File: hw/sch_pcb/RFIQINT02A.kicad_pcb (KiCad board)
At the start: 2 copper layers, 40.1 x 60.5 mm, 33 parts, among them J1 HEADER_2x03_PARALLEL, J2 HEADER_2x04_PARALLEL, J3 SATA7-67491-1030, J4 SATA7-67491-1030, J5 SATA7-67491-1030, J6 RJ45_RJHSE-5384, J7 RJ45_RJHSE-5384, M1 HOLE, M2 HOLE, M3 HOLE, M4 HOLE, U1 Si53322

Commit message: Edit PCB
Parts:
- J1, J2, J3, J4, J5, J6, J7: moved to B.Cu
- moved M2 166.2 mm to (5.08, -55.9)
- moved C10 151.8 mm to (30.5, -53.0), turned to 90 degrees
- moved C1 150.8 mm to (10.3, -47.1), turned to 90 degrees
- moved C9 150.5 mm to (14.9, -40.7), turned to 90 degrees
- moved U1 149.0 mm to (13.1, -32.3)
- moved L1 148.3 mm to (9.84, -25.4)
- moved J2 148.3 mm to (4.95, -45.7)
- moved C8 147.9 mm to (17.4, -40.7), turned to 90 degrees
- moved R4 146.7 mm to (18.4, -37.2)
- moved D2 145.7 mm to (10.2, -38.6), turned to -90 degrees
- moved C5 144.7 mm to (9.97, -27.6), turned to 180 degrees
- moved D1 143.8 mm to (5.08, -34.3), turned to 90 degrees
- moved C7 142.2 mm to (21.5, -32.1)
- moved R2 141.6 mm to (18.7, -28.6), turned to -90 degrees
- moved R6 140.7 mm to (35.2, -50.8)
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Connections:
- C6 pad 2: /CLKOUT0_P -> /CLKOUT1_P
- C7 pad 2: /CLKOUT0_N -> /CLKOUT1_N
- C8 pad 2: /CLKOUT1_P -> /CLKOUT0_P
- C9 pad 2: /CLKOUT1_N -> /CLKOUT0_N
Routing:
- net VCC: track 0.00 -> 57.1 mm, vias 0 -> 3
- net /ADC4_P: track 0.00 -> 31.0 mm
- net /ADC1_P: track 0.00 -> 27.7 mm, vias 0 -> 1
- net /ADC4_N: track 0.00 -> 27.6 mm
- net /ADC3_P: track 0.00 -> 26.6 mm, vias 0 -> 1
- net /ADC1_N: track 0.00 -> 25.4 mm, vias 0 -> 1
- net /ADC3_N: track 0.00 -> 25.0 mm, vias 0 -> 1
- net /CLKOUT1_P: track 0.00 -> 20.5 mm
- net /ADC2_P: track 0.00 -> 19.4 mm, vias 0 -> 1
- net /ADC2_N: track 0.00 -> 18.1 mm, vias 0 -> 1
- net /CLKOUT0_P: track 0.00 -> 16.4 mm
- net /CLKOUT1_N: track 0.00 -> 16.3 mm
- net /CLKOUT0_N: track 0.00 -> 16.2 mm
- net Net-(D1-Pad1): track 0.00 -> 14.1 mm
- net Net-(C8-Pad1): track 0.00 -> 8.95 mm
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
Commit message: Edit PCB
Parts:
- C1, C10, C11, C2, C3, C4, C5, C6, C7, C8, C9, D1, D2, L1, M2, M4, R1, R2, R3, R4, R5, R6, R7, U1: moved to B.Cu
- J1, J2, J3, J4, J5, J6, J7: moved to F.Cu
- moved M4 164.7 mm to (5.08, -55.8)
- moved J5 54.5 mm to (16.5, -57.7)
- moved M2 50.9 mm to (5.08, -4.97)
- moved J4 47.1 mm to (16.5, -6.88)
- moved C10 45.2 mm to (30.5, -7.83), turned to -90 degrees
- moved R6 40.7 mm to (35.2, -10.1)
- moved J6 34.4 mm to (34.9, -13.2), turned to 90 degrees
- moved C1 33.4 mm to (10.3, -13.7), turned to -90 degrees
- moved J2 30.6 mm to (4.95, -15.1)
- moved J3 24.8 mm to (16.0, -42.8)
- moved C8 20.6 mm to (17.4, -20.1), turned to -90 degrees
- moved C9 20.6 mm to (14.9, -20.1), turned to -90 degrees
- moved D2 16.4 mm to (10.2, -22.2), turned to 90 degrees
- moved C2 15.8 mm to (10.8, -38.3), turned to 90 degrees
- moved C3 14.4 mm to (13.6, -37.6), turned to -90 degrees
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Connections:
- M4 pad 1: Net-(M4-Pad1) -> GND
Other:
- board text added: "ADC 1,2"
- board text added: "ADC 3,4"
- board text added: "CLK"
- board text added: "POWER IN 3V3"
- board text added: "POWER IN ANT"

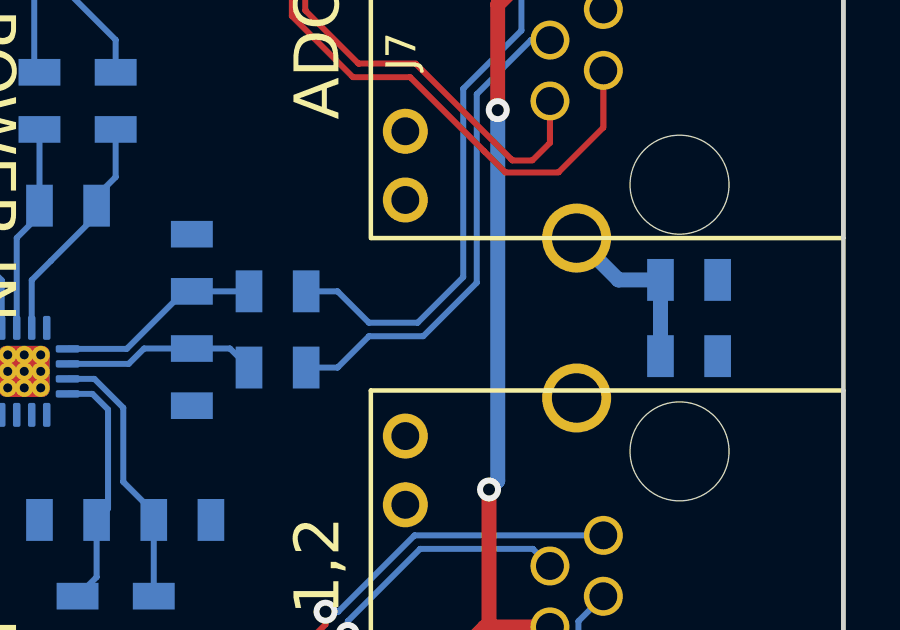
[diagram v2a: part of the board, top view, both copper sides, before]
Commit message: Test of differential pair skew tune.
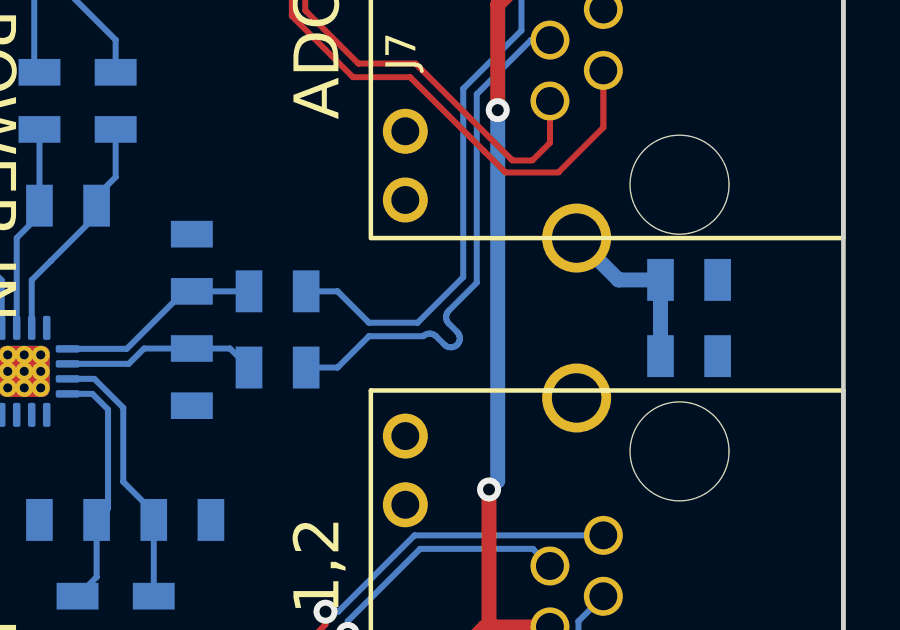
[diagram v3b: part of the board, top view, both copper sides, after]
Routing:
- net /CLKOUT1_N: track 16.3 -> 17.8 mm

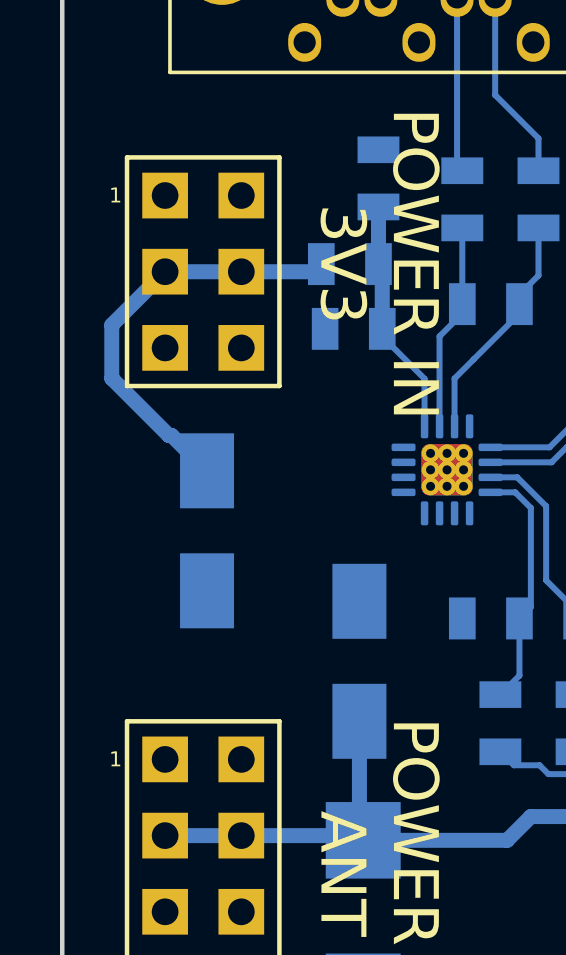
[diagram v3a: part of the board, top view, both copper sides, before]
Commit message: Improve documentation. Generate new image. Remove irrelavant symbols in silkscreen.
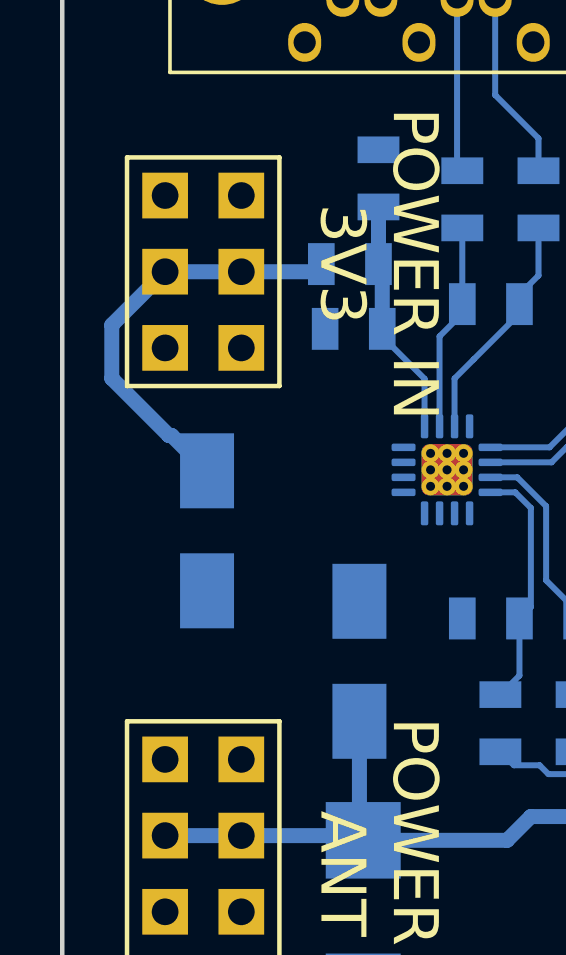
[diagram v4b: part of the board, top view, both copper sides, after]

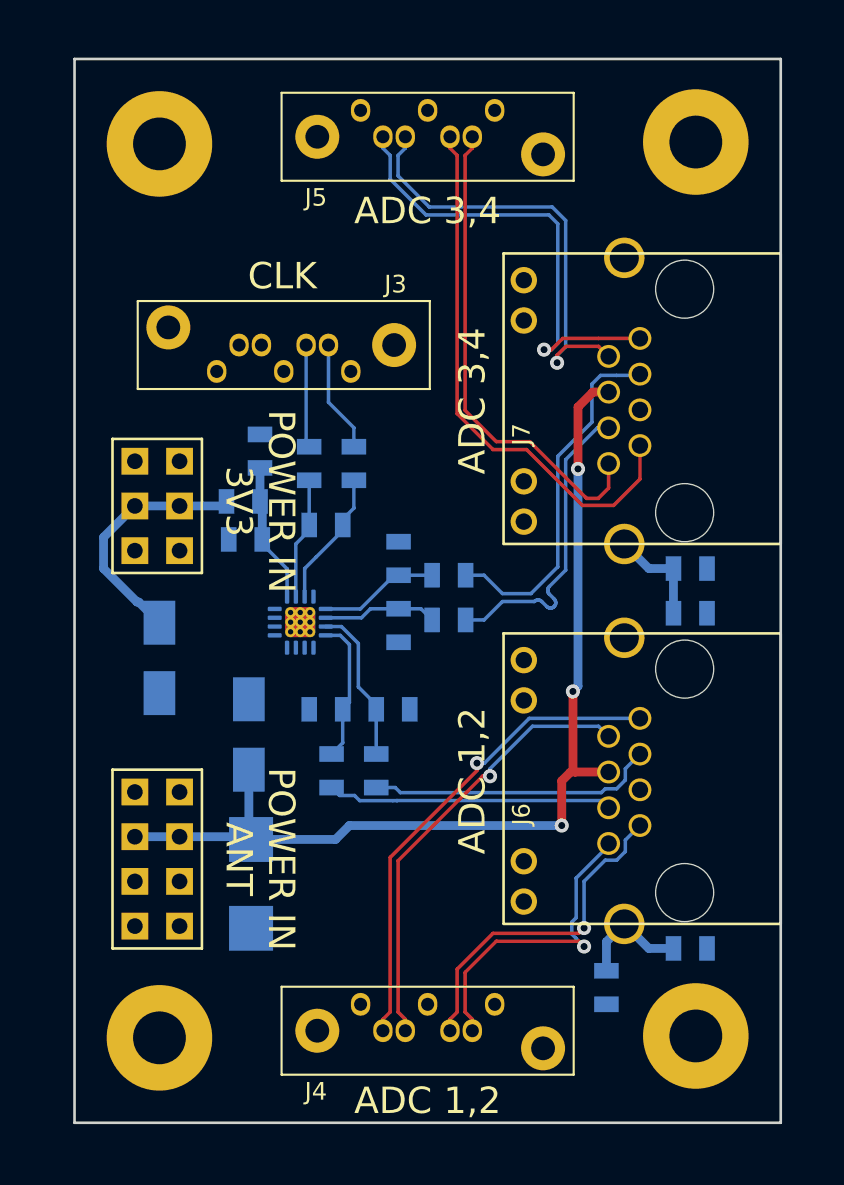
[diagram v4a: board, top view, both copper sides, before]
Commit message: remove vias from differential pairs routing.
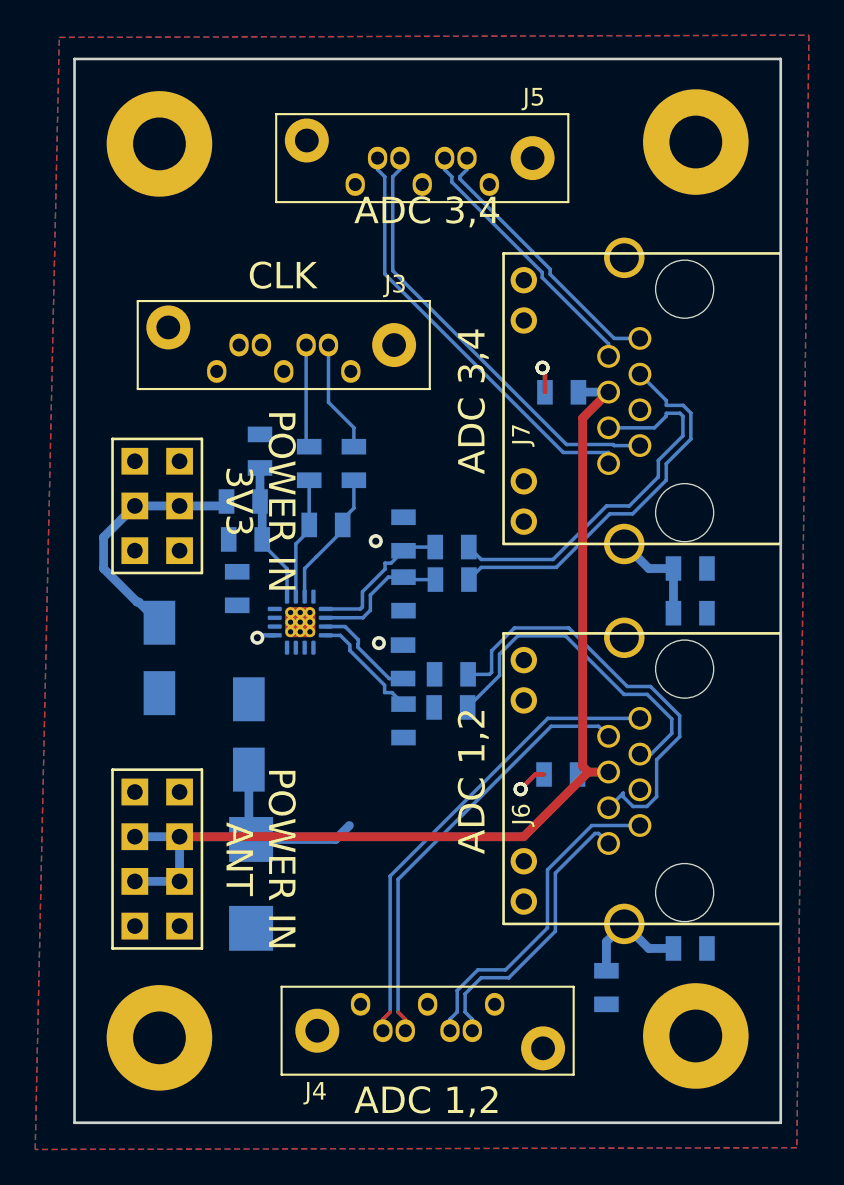
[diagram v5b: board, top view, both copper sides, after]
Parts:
- added C12: 100nF, Mlab_R:SMD-0805, B.Cu at (27.9, -19.9)
- added C13: 100nF, Mlab_R:SMD-0805, B.Cu at (27.9, -41.7)
- added C14: 1uF, Mlab_R:SMD-0805, B.Cu at (9.50, -30.5)
- moved J5 8.44 mm to (23.8, -53.5), turned to 0 degrees
- moved C9 7.68 mm to (21.6, -23.7), turned to 0 degrees
- moved C8 6.94 mm to (21.7, -25.6), turned to 0 degrees
- moved R5 4.46 mm to (18.9, -23.0), turned to -90 degrees
- moved R4 2.76 mm to (18.9, -26.3), turned to 90 degrees
- moved C7 2.30 mm to (21.7, -31.0)
- moved R3 1.82 mm to (18.9, -30.2)
- moved C6 1.61 mm to (21.7, -32.9)
- moved R2 1.42 mm to (18.9, -33.6)
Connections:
- net Net-(C3-Pad1) renamed /CLKIN_P
- net Net-(C3-Pad2) renamed /CLK_P
- net Net-(C4-Pad1) renamed /CLKIN_N
- net Net-(C4-Pad2) renamed /CLK_N
- net Net-(C6-Pad1) renamed /Q0_P
- net Net-(C7-Pad1) renamed /Q0_N
- net Net-(C8-Pad1) renamed /Q1_P
- net Net-(C9-Pad1) renamed /Q1_N
- J3 pad 5: Net-(J3-Pad5) -> unconnected-(J3-Pad5)
- J3 pad 6: Net-(J3-Pad6) -> unconnected-(J3-Pad6)
- J6 pad 10: Net-(J6-Pad10) -> unconnected-(J6-Pad10)
- J6 pad 11: Net-(J6-Pad11) -> unconnected-(J6-Pad11)
- J6 pad 12: Net-(J6-Pad12) -> unconnected-(J6-Pad12)
- J6 pad 3: /CLKOUT0_P -> /CLKOUT0_N
- J6 pad 6: /CLKOUT0_N -> /CLKOUT0_P
- J6 pad 9: Net-(J6-Pad9) -> unconnected-(J6-Pad9)
- J7 pad 10: Net-(J7-Pad10) -> unconnected-(J7-Pad10)
- J7 pad 11: Net-(J7-Pad11) -> unconnected-(J7-Pad11)
- J7 pad 12: Net-(J7-Pad12) -> unconnected-(J7-Pad12)
- J7 pad 3: /CLKOUT1_P -> /CLKOUT1_N
- J7 pad 6: /CLKOUT1_N -> /CLKOUT1_P
- J7 pad 9: Net-(J7-Pad9) -> unconnected-(J7-Pad9)
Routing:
- net VCC: track 57.1 -> 73.5 mm, vias 3 -> 0
- net /ADC3_P: track 26.6 -> 15.5 mm, vias 1 -> 0
- net /ADC3_N: track 25.0 -> 15.1 mm, vias 1 -> 0
- net /CLKOUT0_P: track 16.4 -> 24.8 mm
- net GND: track 0.00 -> 7.31 mm, vias 0 -> 7
- net /ADC4_P: track 31.0 -> 24.7 mm
- net /CLKOUT1_N: track 17.8 -> 22.0 mm
- net /ADC4_N: track 27.6 -> 24.3 mm
- net /Q1_P: track 8.95 -> 5.86 mm
- net /CLKOUT0_N: track 16.2 -> 19.1 mm
- net /Q0_P: track 6.84 -> 8.83 mm
- net /Q1_N: track 8.20 -> 6.42 mm
- net /ADC2_N: track 18.1 -> 16.4 mm, vias 1 -> 0
- net /CLKOUT1_P: track 20.5 -> 21.8 mm
- net /Q0_N: track 6.52 -> 7.75 mm
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- added copper zone on B.Cu, net GND
- added copper zone on F.Cu, net GND

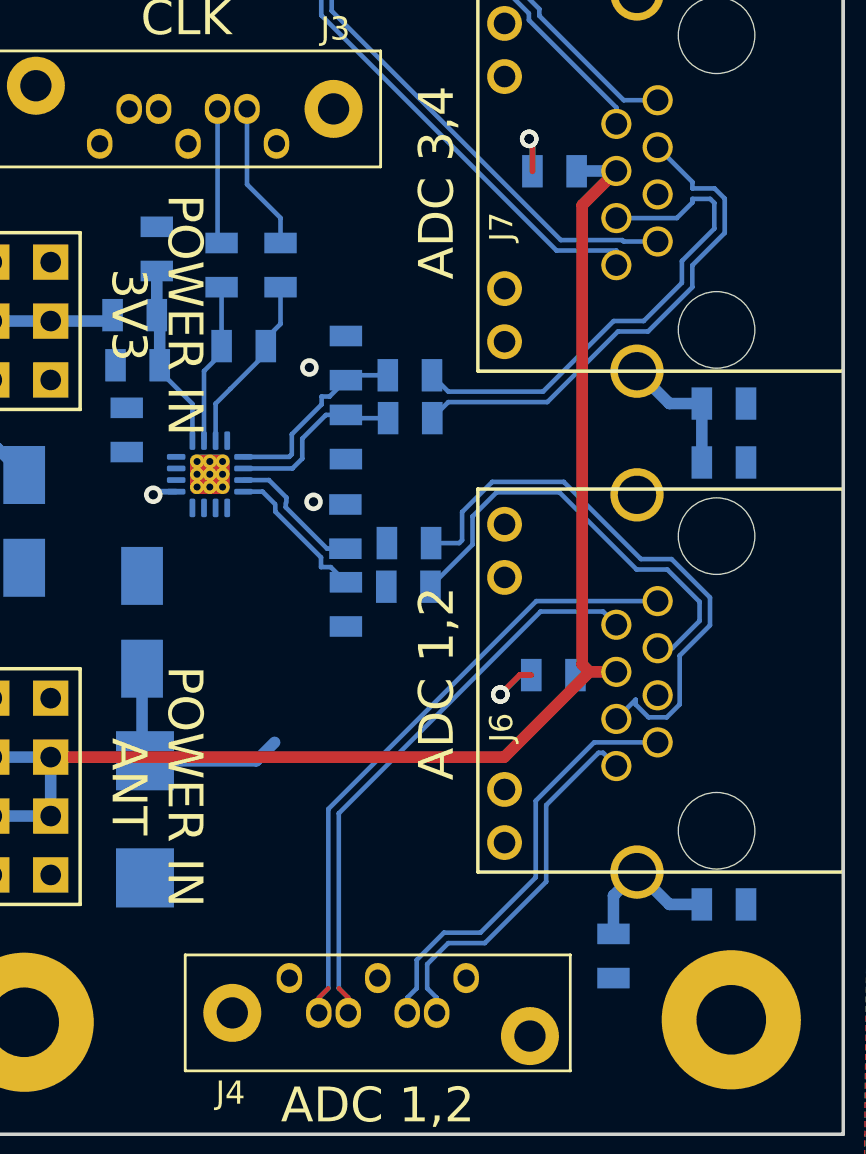
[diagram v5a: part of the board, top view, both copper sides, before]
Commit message: Update net classes.
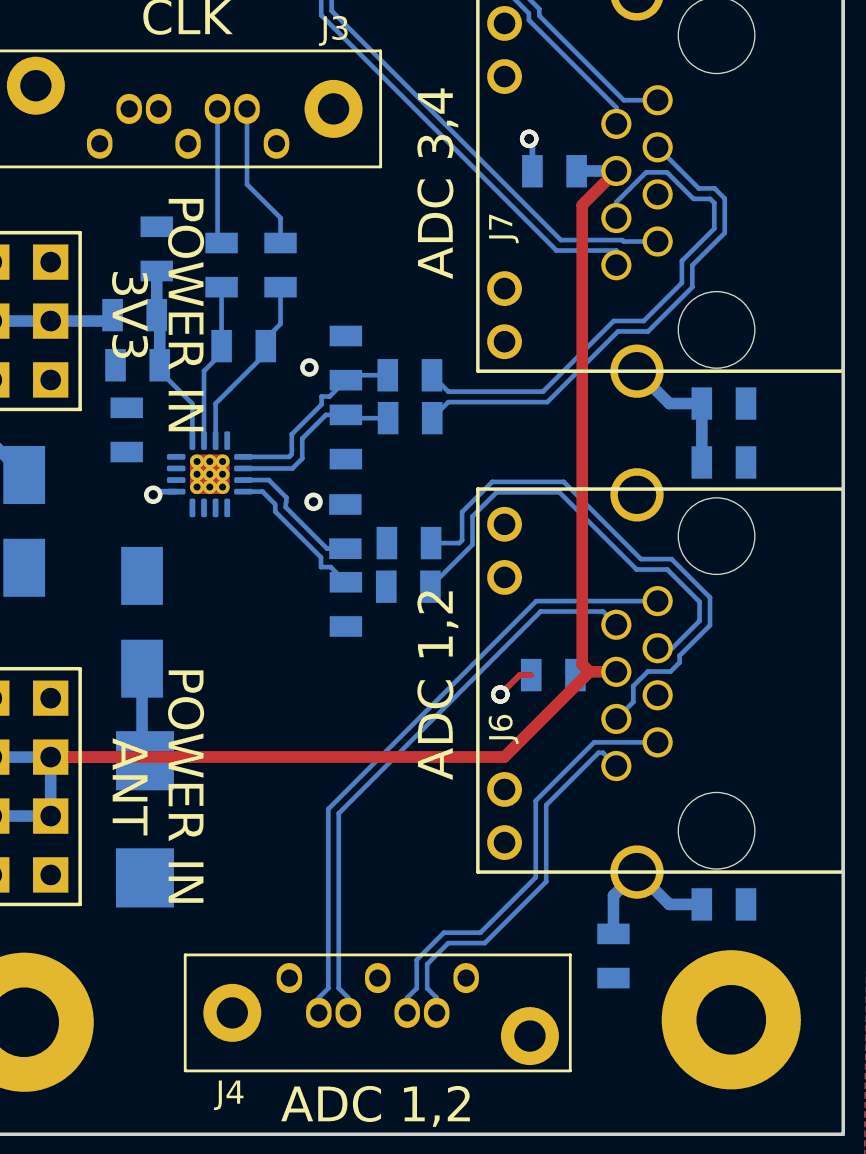
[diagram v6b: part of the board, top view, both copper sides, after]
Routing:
- net VCC: track 73.5 -> 67.5 mm
- net /CLKOUT0_P: track 24.8 -> 23.4 mm
- net GND: track 7.31 -> 6.06 mm
- net /CLKOUT1_P: track 21.8 -> 23.0 mm
- net /ADC1_P: track 28.1 -> 26.9 mm
- net /ADC1_N: track 25.8 -> 24.6 mm
